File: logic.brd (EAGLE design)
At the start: 37.8 x 80 mm, 86 parts, among them CON11 PINHEAD_1X03-2, CON12 PINHEAD_1X03-2, CON2 PINHEAD_2X02-PTH-2-MALE, CON3 PINHEAD_2X04-PLS-2, CON4 CON-3P-TABS, CON5 PINHEAD_2X02-PTH-2-MALE, CON6 PINHEAD_2X02-PTH-2-MALE, CON7 PINHEAD_2X02-PTH-2-MALE, IC1 STM32F105RCT6, IC10 LM75-TSSOP8, IC11 LM75-TSSOP8, IC2 CAT24C02, IC3 NCV8603SN33, IC4 TPS62160QDSGRQ1, IC6 ZXCT1051, IC7 ST3232, IC8 LM75-TSSOP8, IC9 LM5008-MSOP8, X1 24MHz

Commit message: attribute updates
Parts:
- IC3: value NCV8603SN33 -> AP2127-3.3
- moved C11 23.0 mm to (-6.15, 18.4)
- moved C29 23.0 mm to (-6.15, 16.9)
- moved IC1 11.1 mm to (0.00, 65.8)
- moved L4 0.71 mm to (0.00, 45.0)
- moved L3 0.58 mm to (0.00, 52.0)
- moved L1 0.41 mm to (0.00, 27.0)
- moved R23 0.20 mm to (5.45, 75.0)
- moved R24 0.20 mm to (6.55, 75.0)
- moved R25 0.20 mm to (7.65, 75.0)

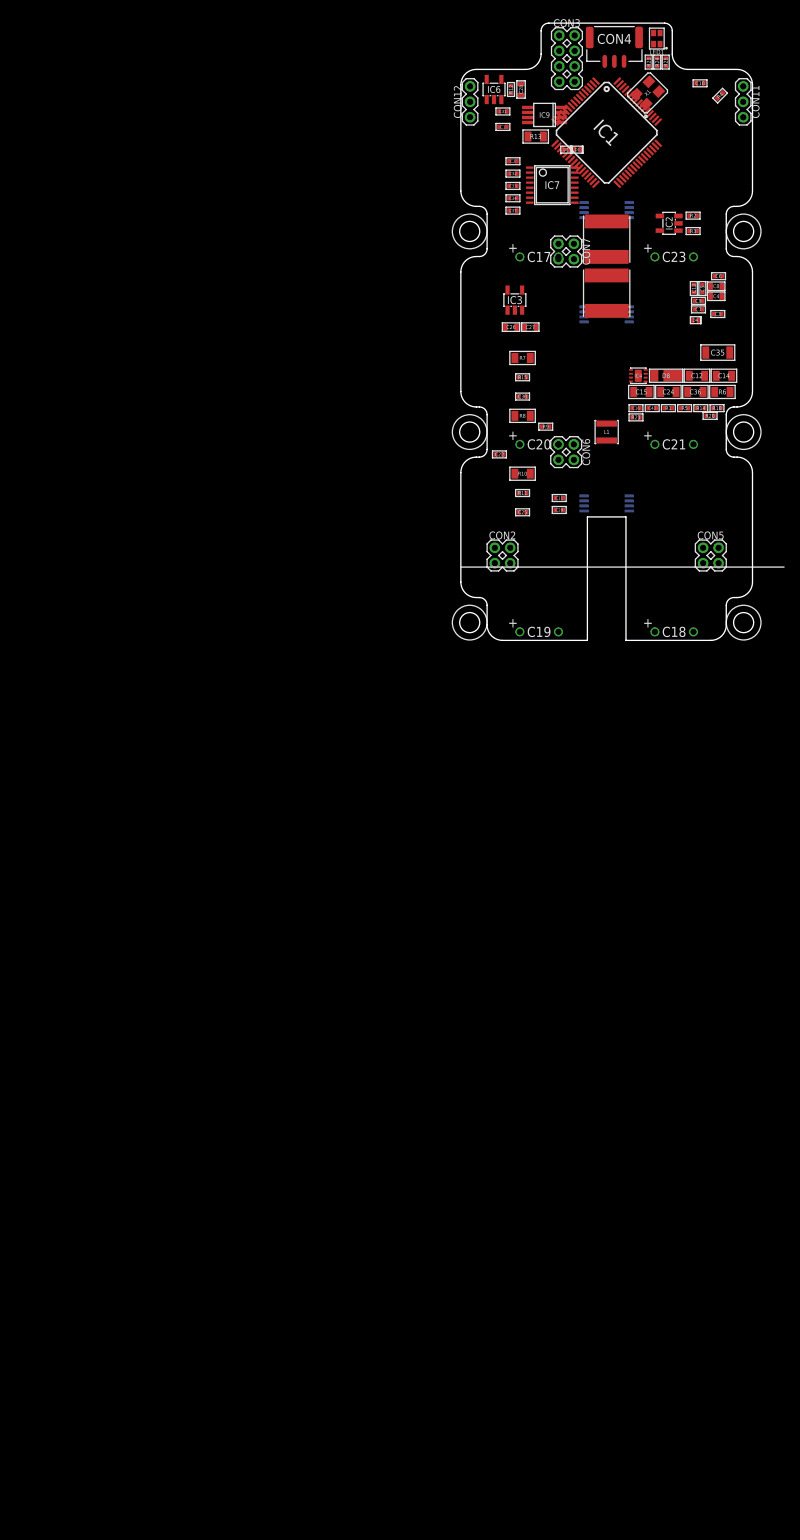
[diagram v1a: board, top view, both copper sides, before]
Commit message: Power supply scheme rearrangement
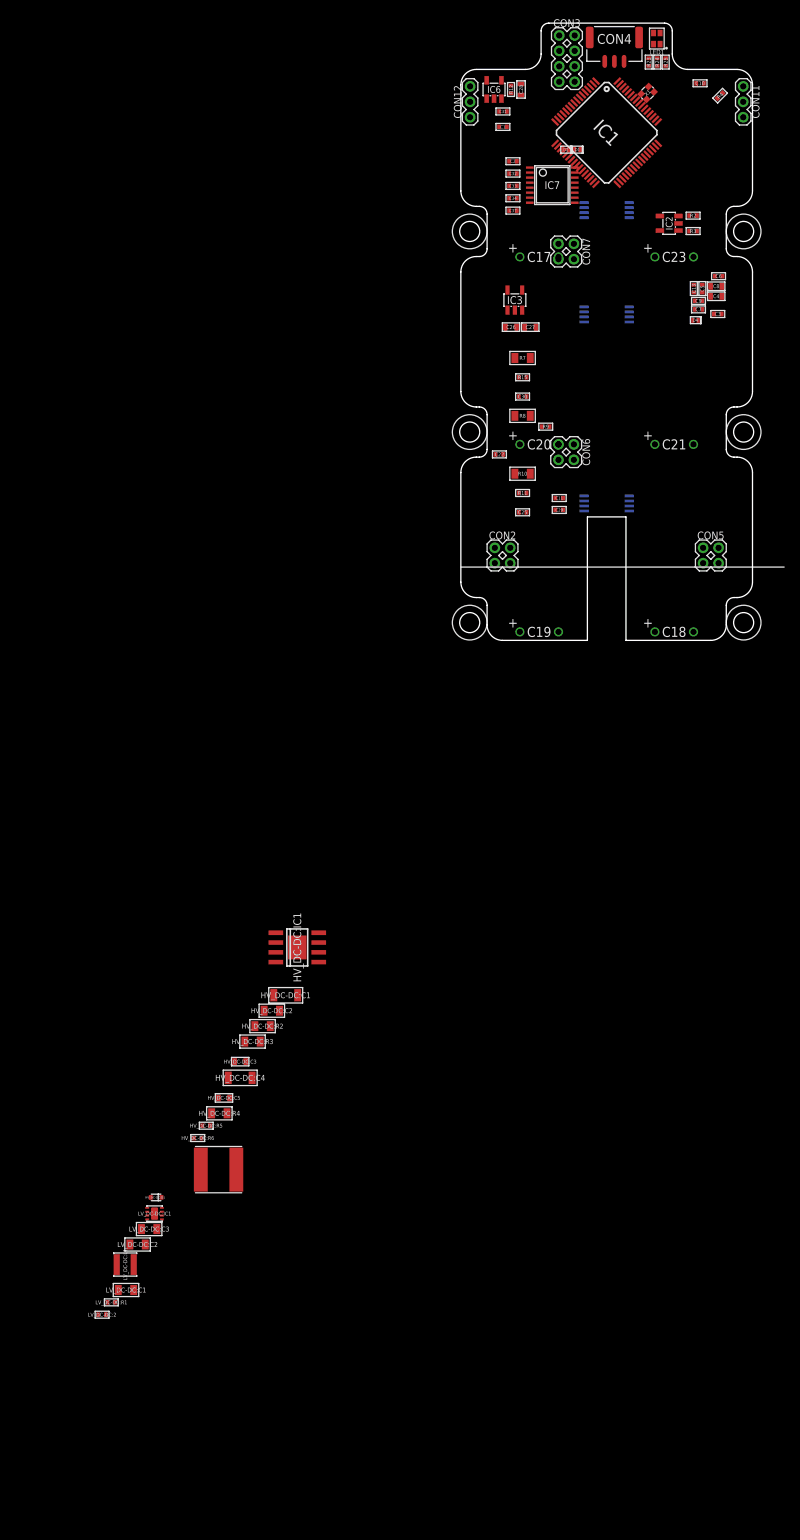
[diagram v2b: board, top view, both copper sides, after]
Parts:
- removed C12, C14, C15, C24: 10uF, rc:C0805
- removed C16: 0.47uF, rc:C0402
- removed C35: 1uF, rc:C1206
- removed C36: 0.1uF, rc:C0805
- removed C43: 0.01uF, rc:C0402
- removed D8: DFLS1100, Diodes:POWERDI-123
- removed IC4: TPS62160QDSGRQ1, dc-dc:WFDFN-8
- removed IC9: LM5008-MSOP8, dc-dc:MSOP8
- removed L1: 2.2µH, power_inductors:NR3015
- removed L3, L4: 100µH, power_inductors:LQS-6028
- removed R1, R14: 51K, rc:R0402
- removed R13, R6: 2R, rc:R0805
- removed R18, R5: 10K, rc:R0402
- removed R20: 287K, rc:R0402
- removed R21: 143K, rc:R0402
- added HV_DC-DC:C1: 2.2uF, rc:C1206
- added HV_DC-DC:C2: 0.47uF, rc:C0805
- added HV_DC-DC:C3, HV_DC-DC:C5: (no value), rc:C0603
- added HV_DC-DC:C4: 22uF, rc:C1206
- added HV_DC-DC:D1: PMEG3005, Diodes:SOD523
- added HV_DC-DC:IC1: LM5017, dc-dc:SOIC8-POWERPAD
- added HV_DC-DC:L1: 100µH, power_inductors:LQS-6028
- added HV_DC-DC:R2: 499K, rc:R0805
- added HV_DC-DC:R3, HV_DC-DC:R4: (no value), rc:R0805
- added HV_DC-DC:R5: 6.98K, rc:R0402
- added HV_DC-DC:R6: 1K, rc:R0402
- added LV_DC-DC:2: 10K, rc:R0402
- added LV_DC-DC:C1, LV_DC-DC:C2, LV_DC-DC:C3: 10uF, rc:C0805
- added LV_DC-DC:IC1: TPS62160QDSGRQ1, dc-dc:WFDFN-8
- added LV_DC-DC:L1: 2.2µH, power_inductors:NR3015
- added LV_DC-DC:R1: 51K, rc:R0402
- IC2: device misc:SOT23-5L@1 -> misc:SOT23-5L
- X1: value 24MHz -> 16MHz; device crystal:OSCILLATOR-3.2X2.5-4P -> crystal:OSCILLATOR-2.0X1.6-4P
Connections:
- removed net N$10: C35.P$2, C36.2, IC9.8, R13.1, R20.2
- removed net N$11: C43.1, IC9.2
- removed net N$13: IC9.3, R21.2
- removed net N$14: C43.2, D8.C, IC9.1, L3.P$1
- removed net N$15: L4.P$2, R1.2, R6.2
- removed net N$17: L3.P$2, L4.P$1
- removed net N$4: IC4.7, L1.1
- removed net N$5: C16.2, IC9.7
- removed net N$50: IC9.5, R1.1, R5.2
- removed net N$8: IC9.6, R20.1
- removed net N$9: IC4.5, R14.1, R18.2
- removed net VDD_15V: C15.2, C24.2, IC4.2, IC4.3, R6.1
- new net HV_DC-DC:N$10: HV_DC-DC:C5.2, HV_DC-DC:D1.C, HV_DC-DC:IC1.6
- new net HV_DC-DC:N$11: HV_DC-DC:IC1.4, HV_DC-DC:R2.2
- new net HV_DC-DC:N$12: HV_DC-DC:C3.1, HV_DC-DC:IC1.7
- new net HV_DC-DC:N$13: HV_DC-DC:C3.2, HV_DC-DC:IC1.8, HV_DC-DC:L1.P$1
- new net HV_DC-DC:N$14: HV_DC-DC:IC1.5, HV_DC-DC:R5.1, HV_DC-DC:R6.2
- new net HV_DC-DC:N$17: HV_DC-DC:IC1.3, HV_DC-DC:R3.1, HV_DC-DC:R4.2
- new net LV_DC-DC:N$1: LV_DC-DC:IC1.7, LV_DC-DC:L1.1
- new net VDC: HV_DC-DC:C1.P$2, HV_DC-DC:C2.2, HV_DC-DC:IC1.2, HV_DC-DC:R2.1, HV_DC-DC:R3.2
- new net VDD_12V: HV_DC-DC:C4.P$2, HV_DC-DC:D1.A, HV_DC-DC:L1.P$2, HV_DC-DC:R5.2, LV_DC-DC:C1.2, LV_DC-DC:IC1.2, LV_DC-DC:IC1.3
- net GND: now also HV_DC-DC:C1.P$1, HV_DC-DC:C2.1, HV_DC-DC:C4.P$1, HV_DC-DC:C5.1, HV_DC-DC:R4.1, HV_DC-DC:R6.1, LV_DC-DC:2.1, LV_DC-DC:2.2, LV_DC-DC:C1.1, LV_DC-DC:C2.1, LV_DC-DC:C3.1, LV_DC-DC:IC1.1, LV_DC-DC:IC1.4, LV_DC-DC:IC1.5, LV_DC-DC:IC1.EP, LV_DC-DC:R1.1; no longer C12.1, C14.1, C15.1, C16.1, C24.1, C35.P$1, C36.1, D8.A, IC4.1, IC4.4, IC4.EP, IC9.4, R18.1, R21.1, R5.1
- net VBAT: no longer R13.2
- net VDD_5V: now also LV_DC-DC:C2.2, LV_DC-DC:C3.2, LV_DC-DC:IC1.6, LV_DC-DC:L1.2, LV_DC-DC:R1.2; no longer C12.2, C14.2, IC4.6, L1.2, R14.2

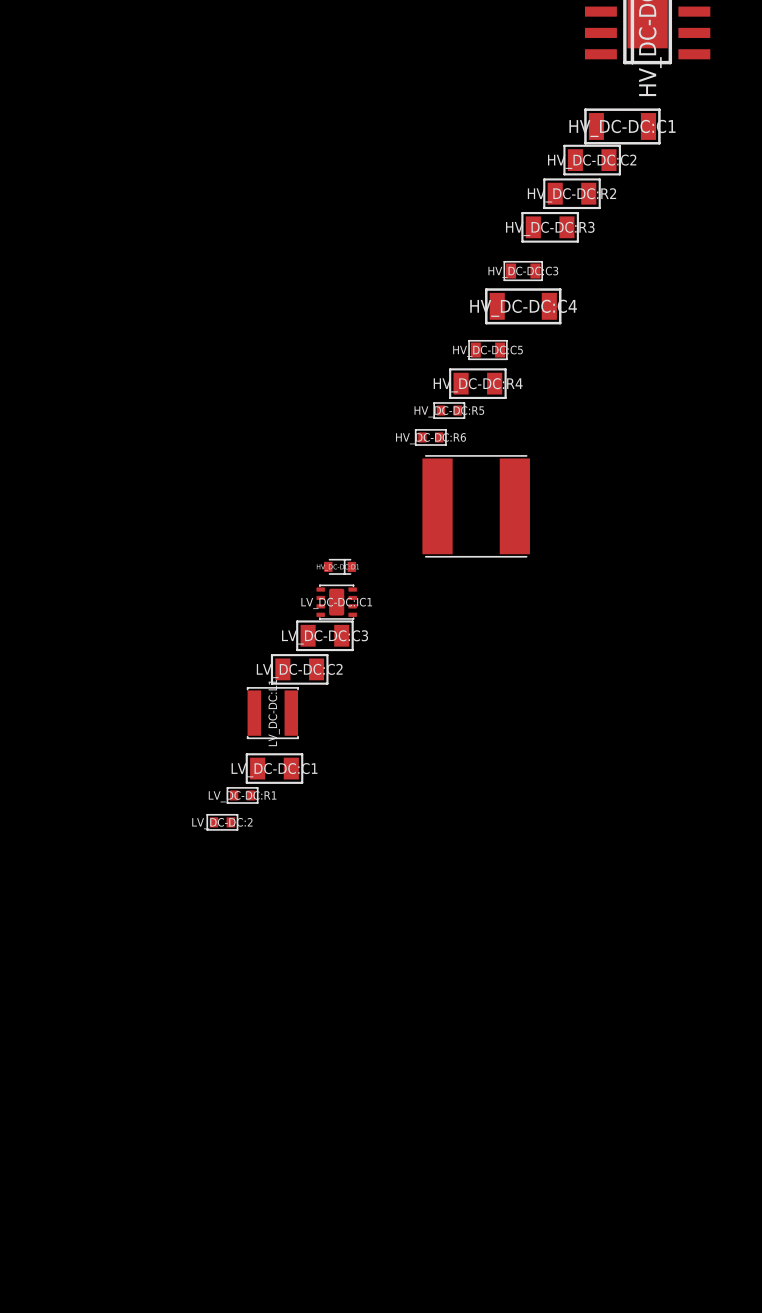
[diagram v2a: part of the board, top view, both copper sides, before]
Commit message: HV dc-dc update
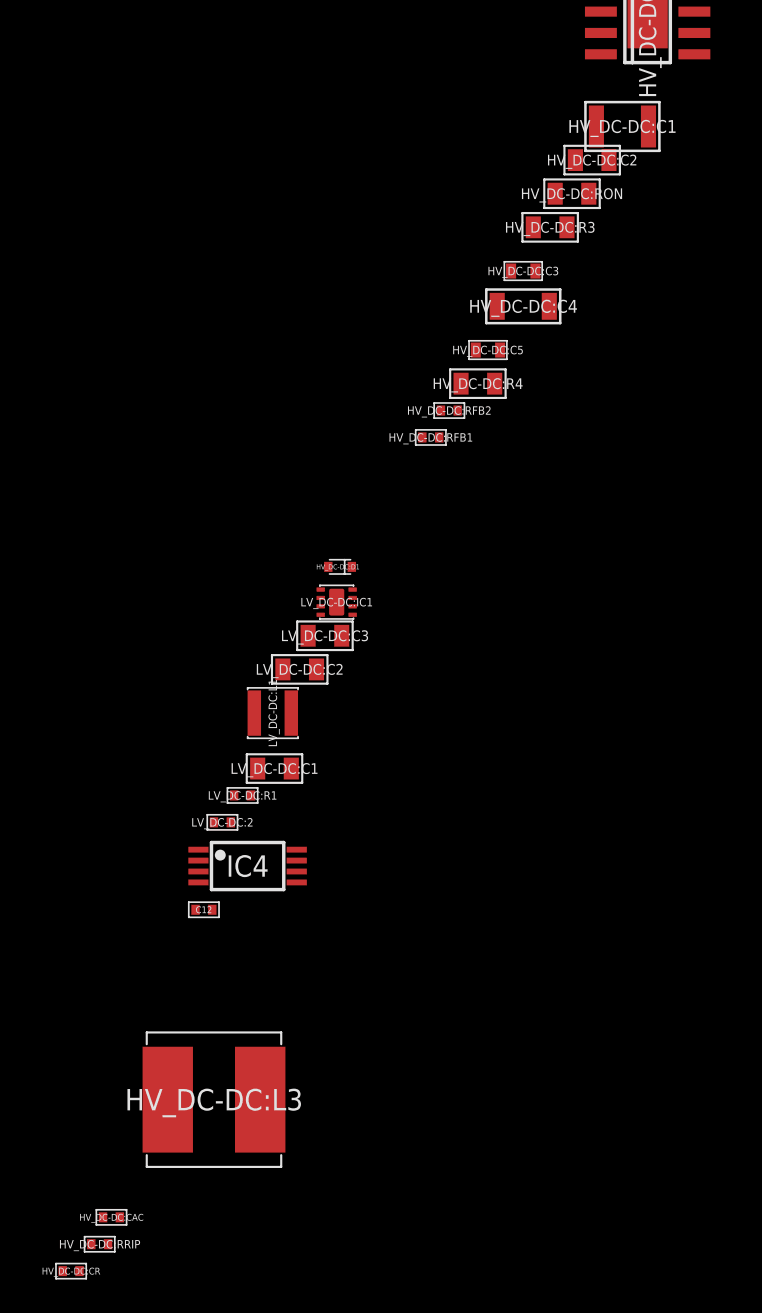
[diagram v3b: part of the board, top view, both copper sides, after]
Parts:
- removed HV_DC-DC:L1: 100µH, power_inductors:LQS-6028
- added C12: 0.1µF, rc:C0402
- added HV_DC-DC:CAC: 0.1uF, rc:C0402
- added HV_DC-DC:CR: 3300pF, rc:C0402
- added HV_DC-DC:L3: 120µH, power_inductors:HPC8040NF
- added HV_DC-DC:RRIP: 110K, rc:R0402
- added IC4: LM75-TSSOP8, misc:TSSOP8
- HV_DC-DC:C1: device rc:C1206 -> rc:C1210
- HV_DC-DC:C3: value (none) -> 0.01uF
- HV_DC-DC:C4: value 22uF -> 10uF
- HV_DC-DC:C5: value (none) -> 1uf
- HV_DC-DC:R3: value (none) -> 127K
- HV_DC-DC:R4: value (none) -> 14K
- HV_DC-DC:RFB2: value 6.98K -> 3K
- HV_DC-DC:RON: value 499K -> 110K
- renumbered HV_DC-DC:R2 to HV_DC-DC:RON, HV_DC-DC:R5 to HV_DC-DC:RFB2, HV_DC-DC:R6 to HV_DC-DC:RFB1
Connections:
- removed net HV_DC-DC:N$13: HV_DC-DC:C3.2, HV_DC-DC:IC1.8, HV_DC-DC:L1.P$1
- new net HV_DC-DC:N$2: HV_DC-DC:C3.2, HV_DC-DC:IC1.8, HV_DC-DC:L3.1, HV_DC-DC:RRIP.2
- new net HV_DC-DC:N$3: HV_DC-DC:CAC.2, HV_DC-DC:CR.2, HV_DC-DC:RRIP.1
- net GND: now also C12.2, HV_DC-DC:C1.1, HV_DC-DC:IC1.1, HV_DC-DC:IC1.P$1, IC4.4; no longer HV_DC-DC:C1.P$1
- net HV_DC-DC:N$14: now also HV_DC-DC:CAC.1
- net I2C_SCL: now also IC4.2
- net I2C_SDA: now also IC4.1
- net VDC: now also HV_DC-DC:C1.2; no longer HV_DC-DC:C1.P$2
- net VDD_12V: now also HV_DC-DC:CR.1, HV_DC-DC:L3.2; no longer HV_DC-DC:L1.P$2
- net VDD_3V3: now also C12.1, IC4.5, IC4.6, IC4.7, IC4.8
